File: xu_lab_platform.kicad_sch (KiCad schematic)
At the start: 0 parts

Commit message: Add schematic files for MCUA
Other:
- added sheet MCU A (xu_lab_platform_mcu1.kicad_sch)
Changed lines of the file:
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@@
 		(company "CU Boulder Senior Design Team 29 - Xu Lab")
+	)
+	(sheet
+		(at 66.04 91.44)
+		(size 38.1 24.13)
+		(exclude_from_sim no)
+		(in_bom yes)
+		(on_board yes)
+		(dnp no)
+		(fields_autoplaced yes)
+		(stroke
+			(width 0.1524)
+			(type solid)
+		)
+		(fill
+			(color 0 0 0 0.0000)
+		)
+		(property "Sheetname" "MCU A"
+			(at 66.04 90.7284 0)
+			(effects
+				(font
+					(size 1.27 1.27)
+				)
+				(justify left bottom)
+			)
+		)
+		(property "Sheetfile" "xu_lab_platform_mcu1.kicad_sch"
+			(at 66.04 116.1546 0)
+			(effects
+				(font
+					(size 1.27 1.27)
+				)
+				(justify left top)
+			)
+		)
+		(instances
+			(project "xu_lab_platform"
+				(path "/71bb14ae-b730-4d22-a41d-cf68989dae2d"
+					(page "2")
+				)
+			)
+		)
 	)
 	(sheet_instances

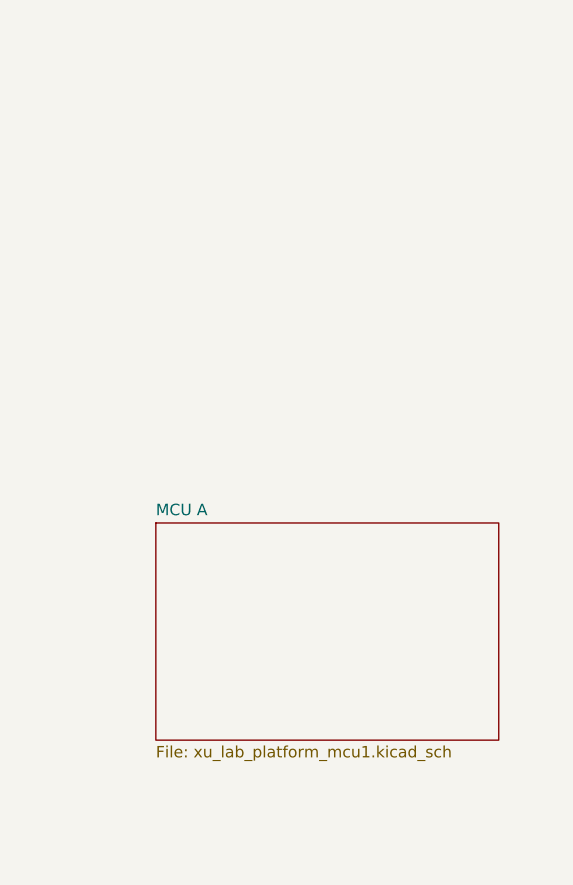
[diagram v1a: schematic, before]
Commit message: Add hierarchical pins for MCU A and update main sheet
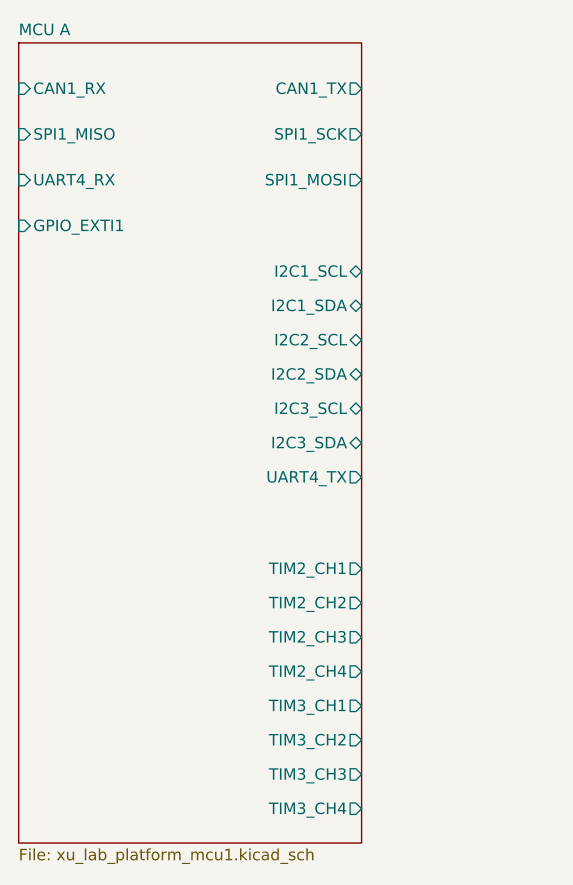
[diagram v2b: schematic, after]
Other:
- sheet MCU A ports: added CAN1_RX, CAN1_TX, GPIO_EXTI1, I2C1_SCL, I2C1_SDA, I2C2_SCL, I2C2_SDA, I2C3_SCL, I2C3_SDA, SPI1_MISO, SPI1_MOSI, SPI1_SCK, TIM2_CH1, TIM2_CH2, TIM2_CH3, TIM2_CH4, TIM3_CH1, TIM3_CH2, TIM3_CH3, TIM3_CH4, UART4_RX, UART4_TX; removed none
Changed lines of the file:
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@@
 	(title_block
 		(title "Main Sheet")
-		(date "2025-10-04")
+		(date "2025-10-15")
 		(rev "A")
 		(company "CU Boulder Senior Design Team 29 - Xu Lab")
 	)
 	(sheet
-		(at 66.04 91.44)
-		(size 38.1 24.13)
+		(at 50.8 38.1)
+		(size 38.1 88.9)
 		(exclude_from_sim no)
 		(in_bom yes)
@@
 		)
 		(property "Sheetname" "MCU A"
-			(at 66.04 90.7284 0)
+			(at 50.8 37.3884 0)
 			(effects
 				(font
@@
 		)
 		(property "Sheetfile" "xu_lab_platform_mcu1.kicad_sch"
-			(at 66.04 116.1546 0)
+			(at 50.8 127.5846 0)
 			(effects
 				(font
@@
 			)
 		)
+		(pin "CAN1_RX" input
+			(at 50.8 43.18 180)
+			(effects
+				(font
+					(size 1.27 1.27)
+				)
+				(justify left)
+			)
+		)
+		(pin "CAN1_TX" output
+			(at 88.9 43.18 0)
+			(effects
+				(font
+					(size 1.27 1.27)
+				)
+				(justify right)
+			)
+		)
+		(pin "GPIO_EXTI1" input
+			(at 50.8 58.42 180)
+			(effects
+				(font
+					(size 1.27 1.27)
+				)
+				(justify left)
+			)
+		)
+		(pin "I2C1_SCL" bidirectional
+			(at 88.9 63.5 0)
+			(effects
+				(font
+					(size 1.27 1.27)
+				)
+				(justify right)
+			)
+		)
+		(pin "I2C1_SDA" bidirectional
+			(at 88.9 67.31 0)
+			(effects
+				(font
+					(size 1.27 1.27)
+				)
+				(justify right)
+			)
+		)
+		(pin "I2C2_SCL" bidirectional
+			(at 88.9 71.12 0)
+			(effects
+				(font
+					(size 1.27 1.27)
+				)
+				(justify right)
+			)
+		)
+		(pin "I2C2_SDA" bidirectional
+			(at 88.9 74.93 0)
+			(effects
+				(font
+					(size 1.27 1.27)
+				)
+				(justify right)
+			)
+		)
+		(pin "I2C3_SCL" bidirectional
+			(at 88.9 78.74 0)
+			(effects
+				(font
+					(size 1.27 1.27)
+				)
+				(justify right)
+			)
+		)
+		(pin "I2C3_SDA" bidirectional
+			(at 88.9 82.55 0)
+			(effects
+				(font
+					(size 1.27 1.27)
+				)
+				(justify right)
+			)
+		)
+		(pin "SPI1_MISO" input
+			(at 50.8 48.26 180)
+			(effects
+				(font
+					(size 1.27 1.27)
+				)
+				(justify left)
+			)
+		)
+		(pin "SPI1_MOSI" output
+			(at 88.9 53.34 0)
+			(effects
+				(font
+					(size 1.27 1.27)
+				)
+				(justify right)
+			)
+		)
+		(pin "SPI1_SCK" output
+			(at 88.9 48.26 0)
+			(effects
+				(font
+					(size 1.27 1.27)
+				)
+				(justify right)
+			)
+		)
+		(pin "TIM2_CH1" output
+			(at 88.9 96.52 0)
+			(effects
+				(font
+					(size 1.27 1.27)
+				)
+				(justify right)
+			)
+		)
+		(pin "TIM2_CH2" output
+			(at 88.9 100.33 0)
+			(effects
+				(font
+					(size 1.27 1.27)
+				)
+				(justify right)
+			)
+		)
+		(pin "TIM2_CH3" output
+			(at 88.9 104.14 0)
+			(effects
+				(font
+					(size 1.27 1.27)
+				)
+				(justify right)
+			)
+		)
+		(pin "TIM2_CH4" output
+			(at 88.9 107.95 0)
+			(effects
+				(font
+					(size 1.27 1.27)
+				)
+				(justify right)
+			)
+		)
+		(pin "TIM3_CH1" output
+			(at 88.9 111.76 0)
+			(effects
+				(font
+					(size 1.27 1.27)
+				)
+				(justify right)
+			)
+		)
+		(pin "TIM3_CH2" output
+			(at 88.9 115.57 0)
+			(effects
+				(font
+					(size 1.27 1.27)
+				)
+				(justify right)
+			)
+		)
+		(pin "TIM3_CH3" output
+			(at 88.9 119.38 0)
+			(effects
+				(font
+					(size 1.27 1.27)
+				)
+				(justify right)
+			)
+		)
+		(pin "TIM3_CH4" output
+			(at 88.9 123.19 0)
+			(effects
+				(font
+					(size 1.27 1.27)
+				)
+				(justify right)
+			)
+		)
+		(pin "UART4_RX" input
+			(at 50.8 53.34 180)
+			(effects
+				(font
+					(size 1.27 1.27)
+				)
+				(justify left)
+			)
+		)
+		(pin "UART4_TX" output
+			(at 88.9 86.36 0)
+			(effects
+				(font
+					(size 1.27 1.27)
+				)
+				(justify right)
+			)
+		)

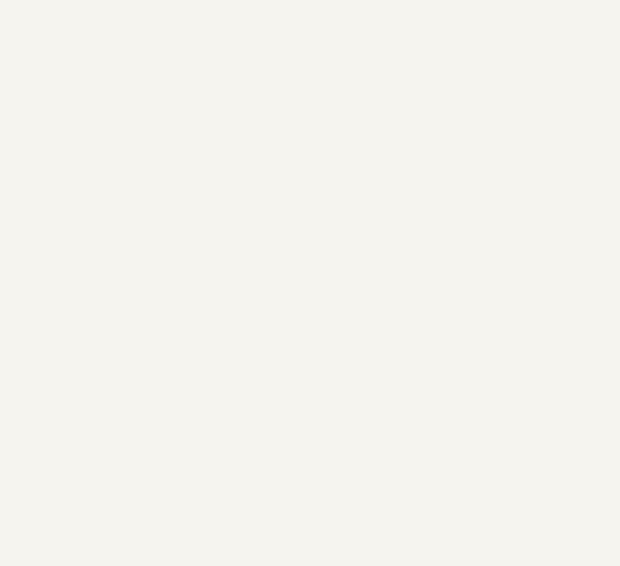
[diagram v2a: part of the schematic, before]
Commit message: Add hierarchical sheet for attitude and heading sensors
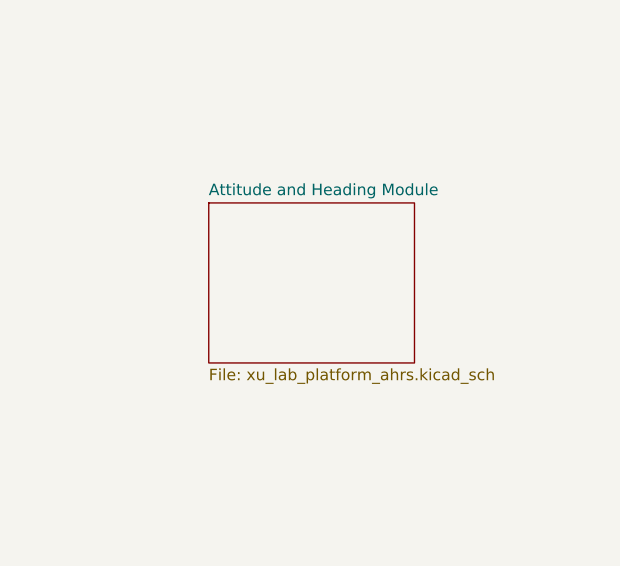
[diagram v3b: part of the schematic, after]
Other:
- added sheet Attitude and Heading Module (xu_lab_platform_ahrs.kicad_sch)
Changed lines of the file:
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@@
+		)
+	)
+	(sheet
+		(at 170.18 55.88)
+		(size 22.86 17.78)
+		(exclude_from_sim no)
+		(in_bom yes)
+		(on_board yes)
+		(dnp no)
+		(fields_autoplaced yes)
+		(stroke
+			(width 0.1524)
+			(type solid)
+		)
+		(fill
+			(color 0 0 0 0.0000)
+		)
+		(property "Sheetname" "Attitude and Heading Module"
+			(at 170.18 55.1684 0)
+			(effects
+				(font
+					(size 1.27 1.27)
+				)
+				(justify left bottom)
+			)
+		)
+		(property "Sheetfile" "xu_lab_platform_ahrs.kicad_sch"
+			(at 170.18 74.2446 0)
+			(effects
+				(font
+					(size 1.27 1.27)
+				)
+				(justify left top)
+			)
+		)
+		(instances
+			(project "xu_lab_platform"
+				(path "/71bb14ae-b730-4d22-a41d-cf68989dae2d"
+					(page "3")
+				)
+			)
 		)
 	)

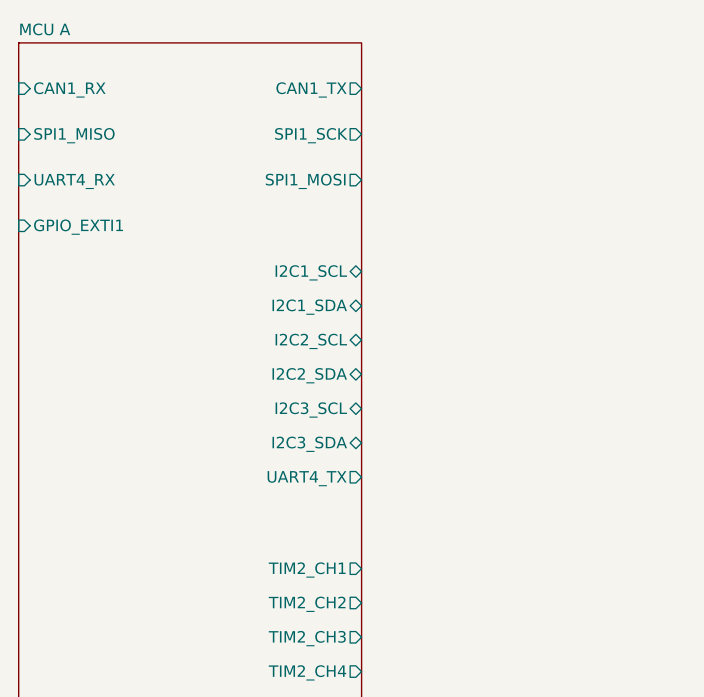
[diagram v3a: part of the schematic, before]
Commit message: Update MCU A pin configuration with SPI CS and an LED output
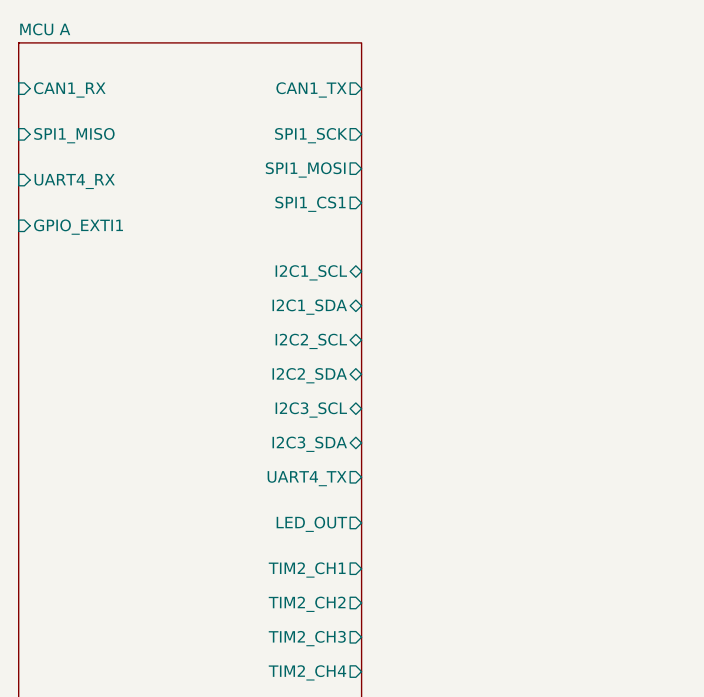
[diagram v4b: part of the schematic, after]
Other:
- sheet MCU A ports: added LED_OUT, SPI1_CS1; removed none
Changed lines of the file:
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@@
 		)
 		(pin "SPI1_MOSI" output
-			(at 88.9 53.34 0)
+			(at 88.9 52.07 0)
 			(effects
 				(font
@@
 			(effects
 				(font
+					(size 1.27 1.27)
+				)
+				(justify right)
+			)
+		)
+		(pin "LED_OUT" output
+			(at 88.9 91.44 0)
+			(effects
+				(font
+					(size 1.27 1.27)
+				)
+				(justify right)
+			)
+		)
+		(pin "SPI1_CS1" output
+			(at 88.9 55.88 0)
+			(effects
+				(font

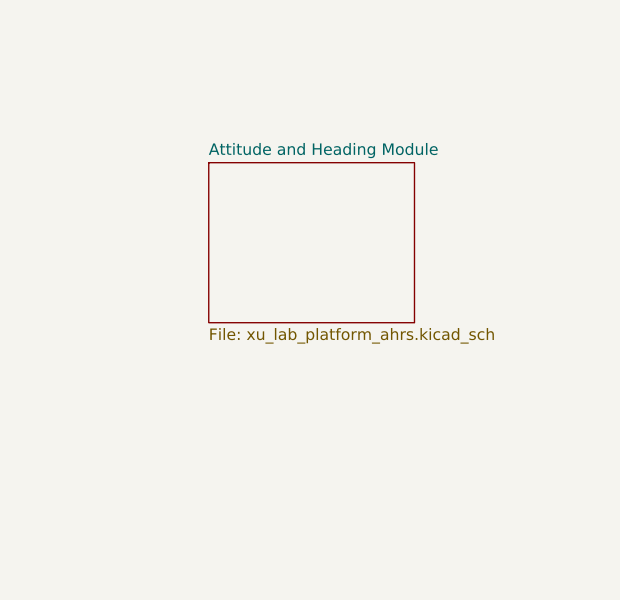
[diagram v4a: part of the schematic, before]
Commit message: Add sensor connections
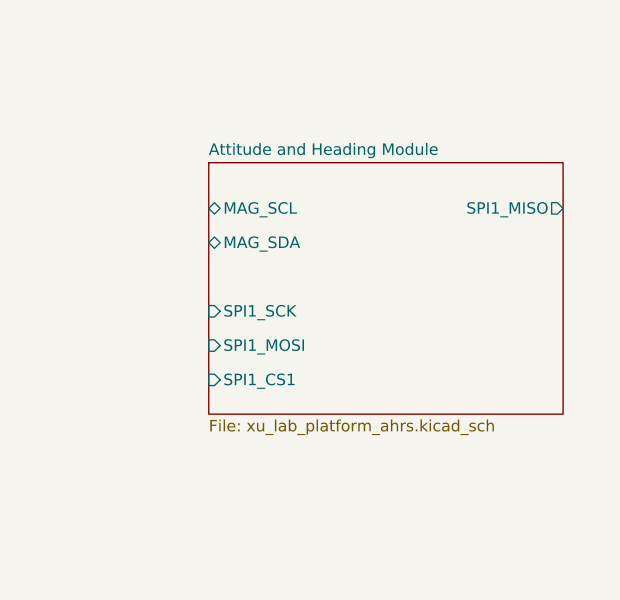
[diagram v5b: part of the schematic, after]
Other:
- sheet Attitude and Heading Module ports: added MAG_SCL, MAG_SDA, SPI1_CS1, SPI1_MISO, SPI1_MOSI, SPI1_SCK; removed none
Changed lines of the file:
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@@
 	(title_block
 		(title "Main Sheet")
-		(date "2025-10-15")
+		(date "2025-10-17")
 		(rev "A")
 		(company "CU Boulder Senior Design Team 29 - Xu Lab")
@@
 	(sheet
 		(at 170.18 55.88)
-		(size 22.86 17.78)
+		(size 39.37 27.94)
 		(exclude_from_sim no)
 		(in_bom yes)
@@
 		)
 		(property "Sheetfile" "xu_lab_platform_ahrs.kicad_sch"
-			(at 170.18 74.2446 0)
+			(at 170.18 84.4046 0)
 			(effects
 				(font
@@
 			)
 		)
+		(pin "MAG_SCL" bidirectional
+			(at 170.18 60.96 180)
+			(effects
+				(font
+					(size 1.27 1.27)
+				)
+				(justify left)
+			)
+		)
+		(pin "MAG_SDA" bidirectional
+			(at 170.18 64.77 180)
+			(effects
+				(font
+					(size 1.27 1.27)
+				)
+				(justify left)
+			)
+		)
+		(pin "SPI1_CS1" input
+			(at 170.18 80.01 180)
+			(effects
+				(font
+					(size 1.27 1.27)
+				)
+				(justify left)
+			)
+		)
+		(pin "SPI1_MISO" output
+			(at 209.55 60.96 0)
+			(effects
+				(font
+					(size 1.27 1.27)
+				)
+				(justify right)
+			)
+		)
+		(pin "SPI1_MOSI" input
+			(at 170.18 76.2 180)
+			(effects
+				(font
+					(size 1.27 1.27)
+				)
+				(justify left)
+			)
+		)
+		(pin "SPI1_SCK" input
+			(at 170.18 72.39 180)
+			(effects
+				(font
+					(size 1.27 1.27)
+				)
+				(justify left)
+			)
+		)

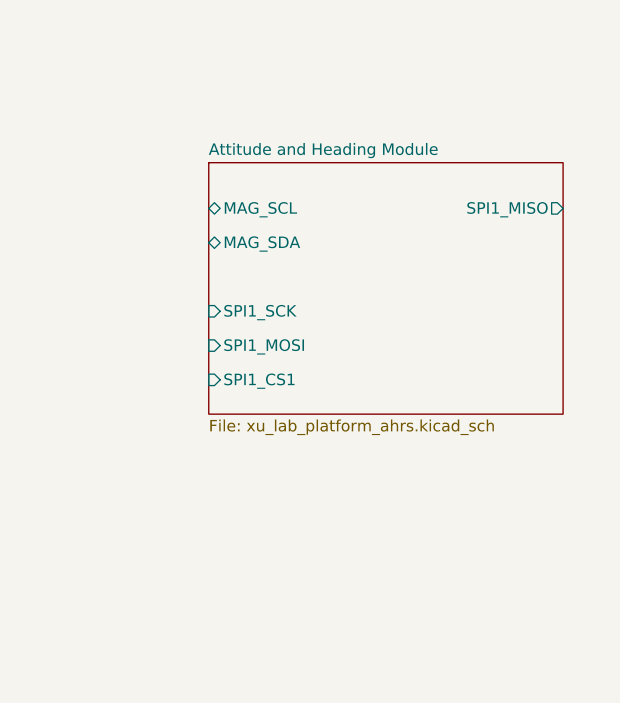
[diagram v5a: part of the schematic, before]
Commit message: Add pressure sensor schematic
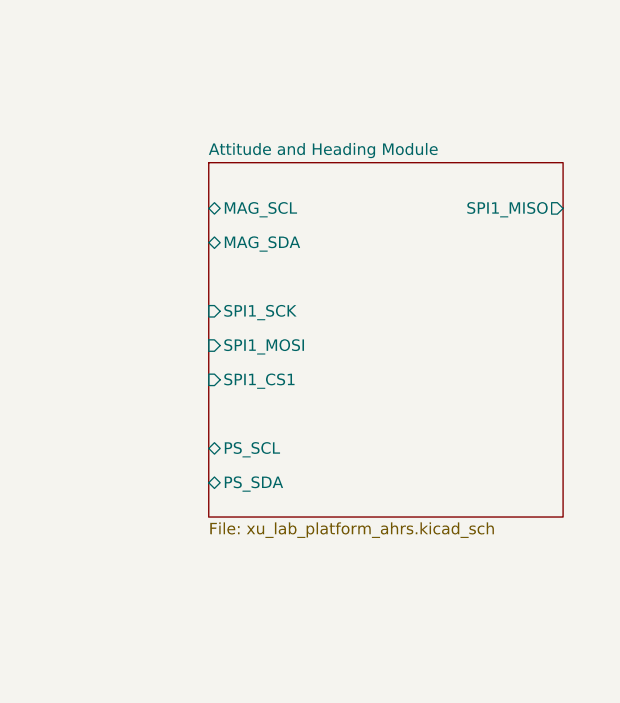
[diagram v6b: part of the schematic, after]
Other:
- sheet Attitude and Heading Module ports: added PS_SCL, PS_SDA; removed none
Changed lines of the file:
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@@
 	(sheet
 		(at 170.18 55.88)
-		(size 39.37 27.94)
+		(size 39.37 39.37)
 		(exclude_from_sim no)
 		(in_bom yes)
@@
 		)
 		(property "Sheetfile" "xu_lab_platform_ahrs.kicad_sch"
-			(at 170.18 84.4046 0)
+			(at 170.18 95.8346 0)
 			(effects
 				(font
@@
 			(effects
 				(font
+					(size 1.27 1.27)
+				)
+				(justify left)
+			)
+		)
+		(pin "PS_SCL" bidirectional
+			(at 170.18 87.63 180)
+			(effects
+				(font
+					(size 1.27 1.27)
+				)
+				(justify left)
+			)
+		)
+		(pin "PS_SDA" bidirectional
+			(at 170.18 91.44 180)
+			(effects
+				(font
